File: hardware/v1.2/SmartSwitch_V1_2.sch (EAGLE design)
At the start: 47 parts, among them K1 FTR-LYC5, K2 FTR-LYC5, U2 AMS1117-3.3

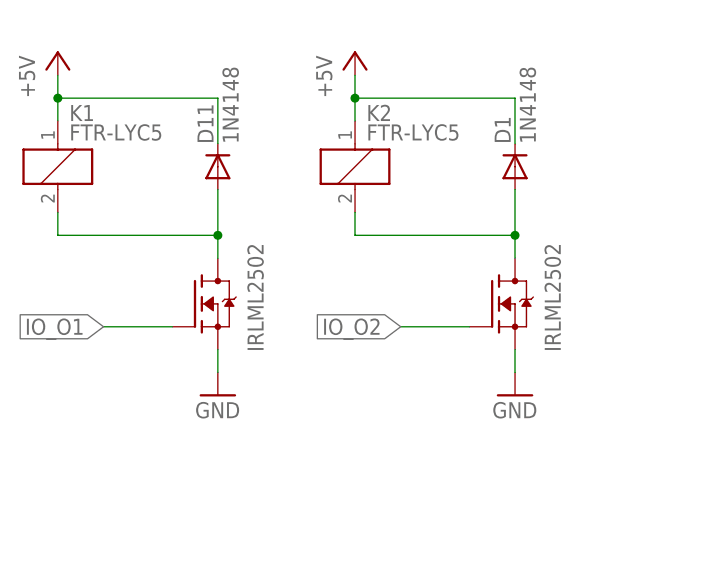
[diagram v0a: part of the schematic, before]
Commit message: Equalization of BOM and Schematic
Mixup of "my" standard driver transistor (IRLML2502, 20V 4,2A) and the used one (IRLML2402, 20V, 1,2A) was adjusted.
Both will work in the given circuit becaus only a coil-current of 35mA is necessary.
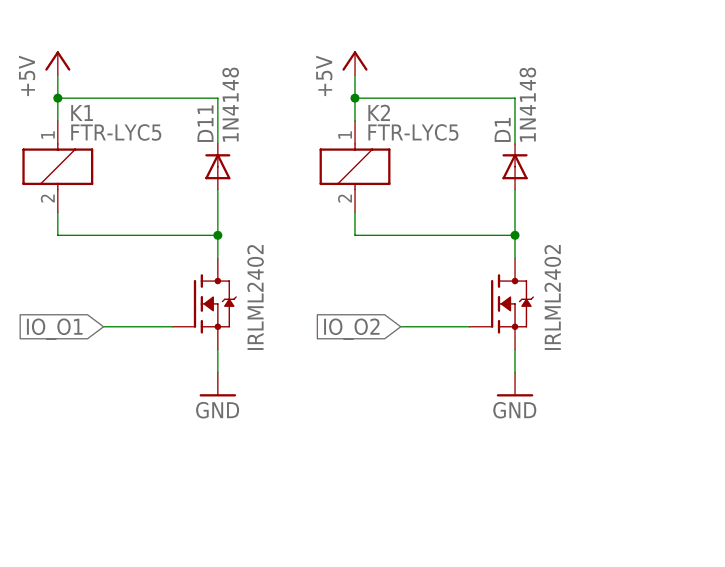
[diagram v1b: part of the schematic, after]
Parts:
- U$7, U$8: value IRLML2502 -> IRLML2402
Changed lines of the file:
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@@
 <part name="P+4" library="supply1" deviceset="+5V" device=""/>
 <part name="P+5" library="supply1" deviceset="+5V" device=""/>
-<part name="U$7" library="transistor-fet" deviceset="IRLML2502" device=""/>
-<part name="U$8" library="transistor-fet" deviceset="IRLML2502" device=""/>
+<part name="U$7" library="transistor-fet" deviceset="IRLML2502" device="" value="IRLML2402"/>
+<part name="U$8" library="transistor-fet" deviceset="IRLML2502" device="" value="IRLML2402"/>
 <part name="GND5" library="supply1" deviceset="GND" device=""/>
 <part name="GND6" library="supply1" deviceset="GND" device=""/>
